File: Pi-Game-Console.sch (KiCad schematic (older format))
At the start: 108 parts, among them J1 Conn_01x02_Female, J10 Conn_01x04_Female, J2 FPC_Connector, J3 Conn_Coaxial, J4 AudioJack3_Ground_SwitchTR, J5 Micro_SD_Card, J6 CAM1, J7 USB_A, J8 USB_A, J9 Conn_01x04_Female, SW1 SW_DIP_x01, SW10 Y_Button, SW11 D_PAD_UP_Button, SW12 D_PAD_DOWN_Button, SW13 D_PAD_LEFT_Button, SW14 D_PAD_RIGHT_Button, SW2 Home_Button, SW3 Start_Button, SW4 Select_Button, SW5 L_Button, SW6 R_Button, SW7 A_Button, SW8 B_Button, SW9 X_Button, U1 UDA1334ATS, U2 TDA2822, U3 FAN5333BSX, U4 AR1100, U5 ATmega32U4-AU, U6 FE1.1s, Y1 12MHz, Y2 16MHz, Y3 12MHz

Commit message: Fixed footprints, added PWM to display backlight
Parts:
- removed D1: 1N4148, Diode_SMD:D_0805_2012Metric, symbol Device:D
- removed J10, J9: Conn_01x04_Female, Connector_Molex:Molex_CLIK-Mate_502585-0470_1x04-1MP_P1.50mm_Horizontal, symbol Connector:Conn_01x04_Female
- removed JP2: SolderJumper_2_Open, Jumper:SolderJumper-2_P1.3mm_Open_TrianglePad1.0x1.5mm, symbol Jumper:SolderJumper_2_Open
- removed R14: 20k, Resistor_SMD:R_0805_2012Metric, symbol Device:R
- removed R18: 67, Resistor_SMD:R_0805_2012Metric, symbol Device:R
- removed RV1: R_POT, Potentiometer_SMD:Potentiometer_Bourns_3214G_Horizontal, symbol Device:R_POT
- added J10, J9: Conn_01x05_Female, Connector_FFC-FPC:Molex_200528-0050_1x05-1MP_P1.00mm_Horizontal, symbol Connector:Conn_01x05_Female
- added RV2: R_POT, Potentiometer_SMD:Potentiometer_Bourns_3269P_Horizontal, symbol Device:R_POT
- SW10, SW11, SW12, SW13, SW14, SW2, SW3, SW4, SW5, SW6, SW7, SW8, SW9: footprint Button_Switch_SMD:SW_Push_1P1T_NO_6x6mm_H9.5mm -> Button_Switch_THT:SW_PUSH_6mm_H5mm
- renumbered D2 to D1, D3 to D2, D4 to D3, JP3 to JP2, R15 to R14, R16 to R15, R17 to R16, R19 to R17, R20 to R18, R21 to R19, R22 to R20, R23 to R21
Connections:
- net +5V: now also J10.1 (Pin_1), J9.1 (Pin_1), RV2.1
- net GND: now also J10.3 (Pin_3), J9.3 (Pin_3), RV2.3
- net L_JOYSTICK_X: now also J9.2 (Pin_2)
- net L_JOYSTICK_Y: now also J9.4 (Pin_4)
- net R_JOYSTICK_X: now also J10.2 (Pin_2)
- net R_JOYSTICK_Y: now also J10.4 (Pin_4)
- net DISP_PWM: now reaches U5.12 (PB7)
- net DISP_PWM: now also U3.4 (~SHDN)
- net DISP_PWM_POT: now reaches U5.40 (PF1)
- net DISP_PWM_POT: now also RV2.2
- net R_JOYSTICK_BTN: now reaches U5.41 (PF0)
- net R_JOYSTICK_BTN: now also J10.5 (Pin_5)
- net L_JOYSTICK_BTN: now reaches U5.8 (PB0)
- net L_JOYSTICK_BTN: now also J9.5 (Pin_5)
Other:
- note added: "DISPLAY BACKLIGHT CONTROL"
- note added: "JOYSTICK PINOUTS ARE NOT YET VALID"
- moved on the sheet: J7, J8, JP2, R17

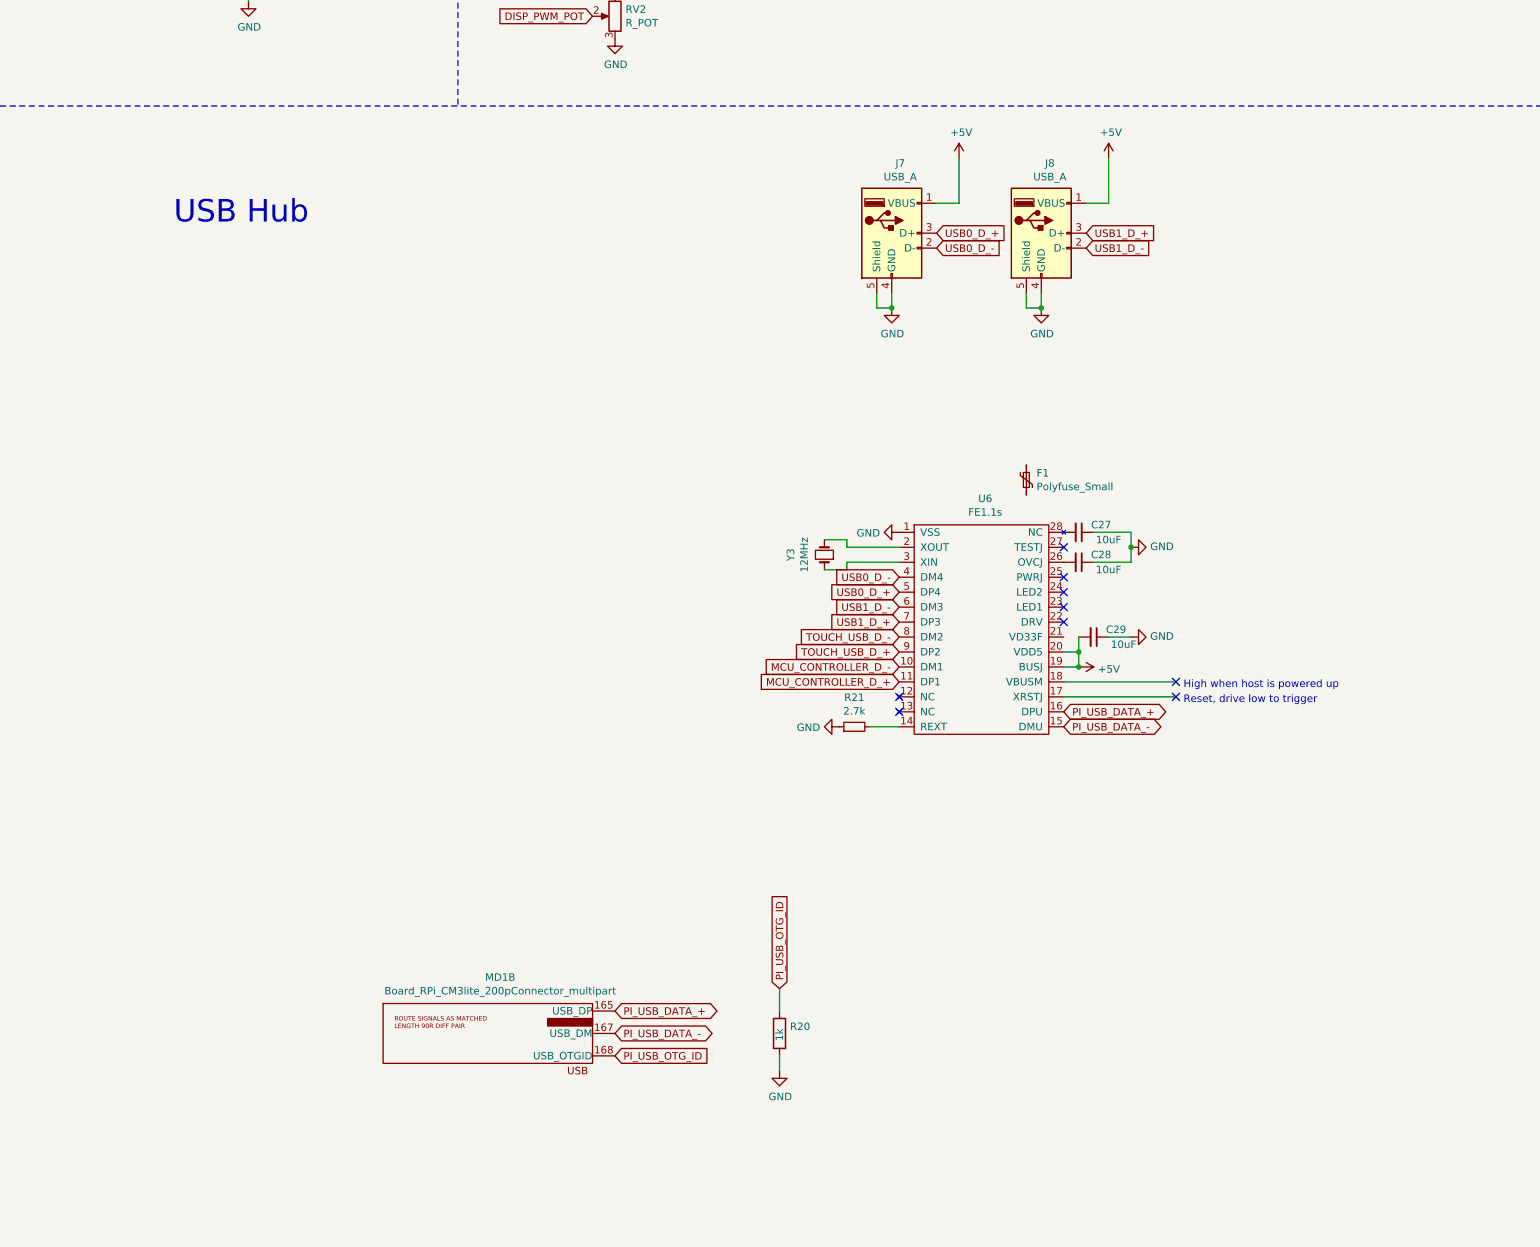
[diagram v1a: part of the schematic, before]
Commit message: Added Buck Converters for Power
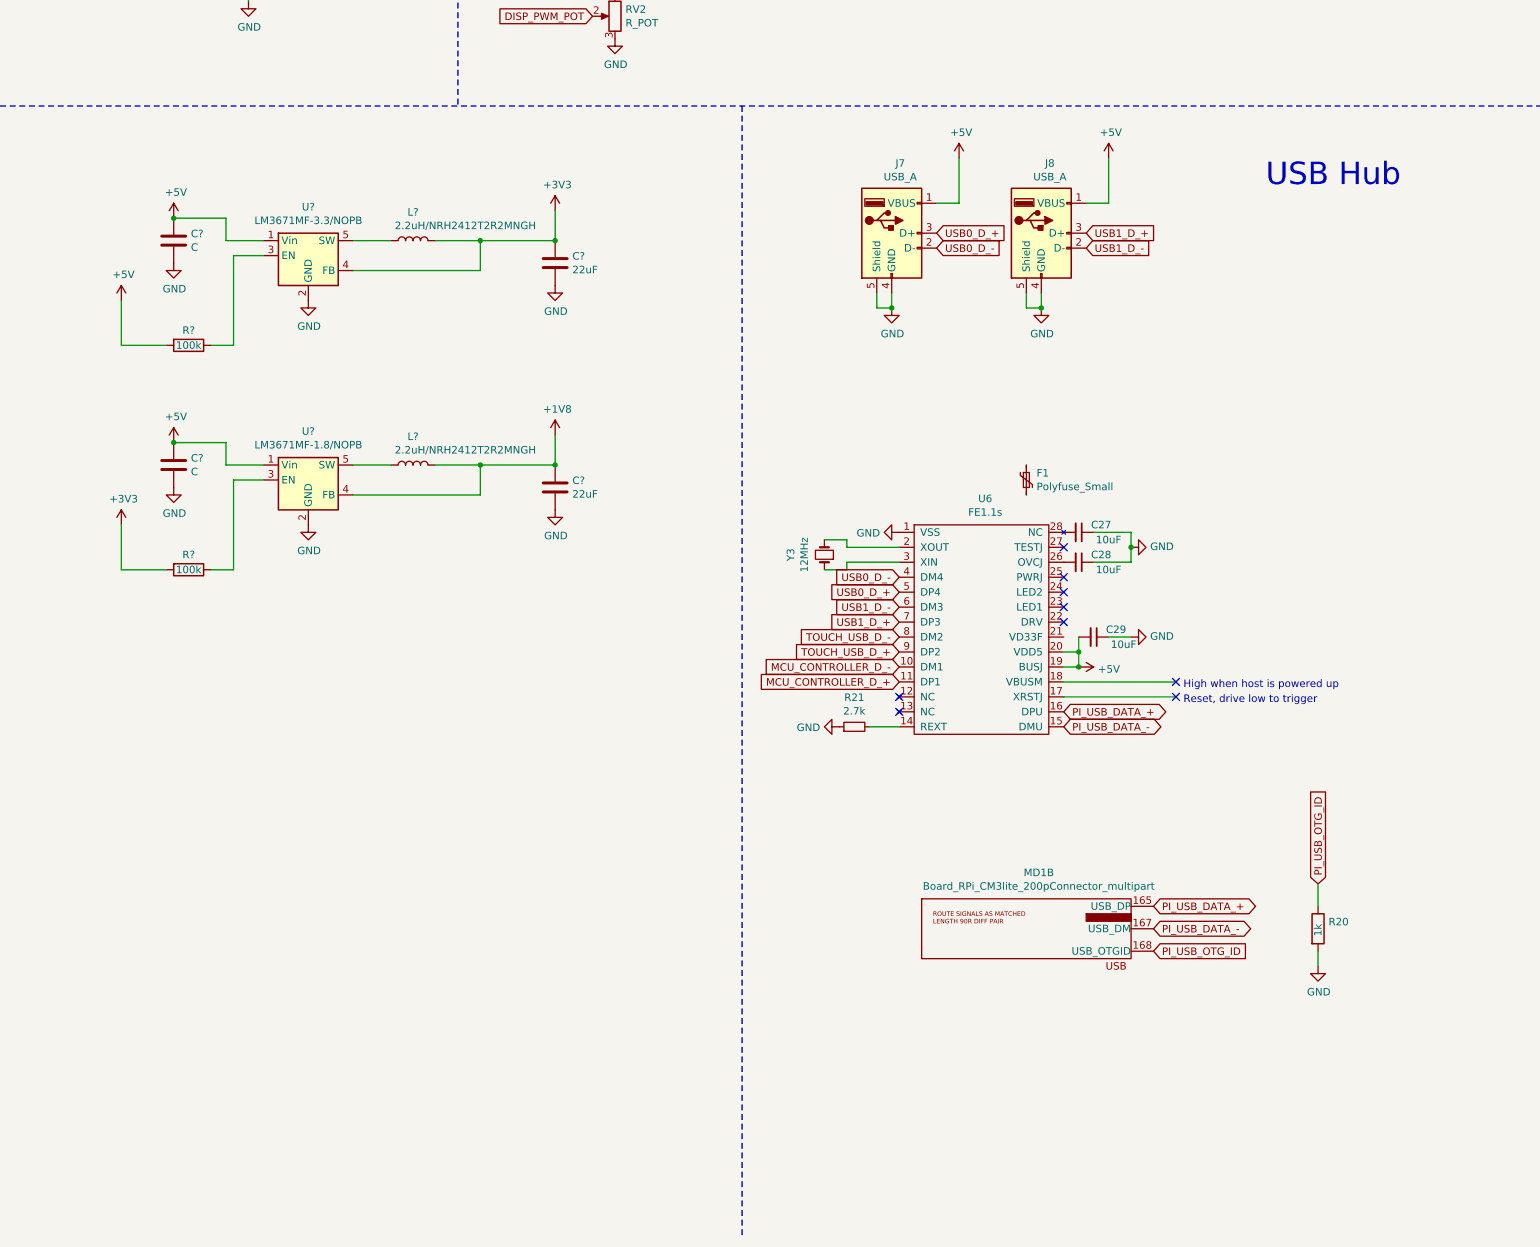
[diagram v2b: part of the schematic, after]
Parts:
- added C? (x2): 22uF, symbol Device:C
- added C? (x2): C, symbol Device:C
- added L? (x2): 2.2uH/NRH2412T2R2MNGH, symbol Device:L
- added R? (x2): 100k, symbol Device:R
- added U?: LM3671MF-3.3/NOPB, Package_TO_SOT_SMD:TSOT-23-5, symbol Regulator_Switching:LM3670MF
- added U?: LM3671MF-1.8/NOPB, Package_TO_SOT_SMD:TSOT-23-5, symbol Regulator_Switching:LM3670MF
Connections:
- net +1V8: now also C?.1, L?.2, U?.4 (FB)
- net +3V3: now also C?.1, L?.2, R?.2, U?.4 (FB)
- net +5V: now also C?.1, C?.1, R?.2, U?.1 (Vin), U?.1 (Vin)
- net GND: now also C?.2, C?.2, C?.2, C?.2, U?.2 (GND), U?.2 (GND)
- new net: R?.1, U?.3 (EN) (x2)
- new net: L?.1, U?.5 (SW) (x2)
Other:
- moved on the sheet: MD1B, R20

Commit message: Updated values for several parts
Mostly capacitors.  Still need to do further review the schematic before it's all the way finished.
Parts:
- C10, C11: value 0.01uF -> 10nF
- C15, C16: value C_Small -> 20pF
- C21, C5, C6: value 0.1uF -> 100nF
- C22, C23: renamed from C?; value C -> 10uF
- C24: renamed from C22; value 0.1uF -> 100nF
- C30: renamed from C26; value C_Small -> 10uF
- gave numbers to parts that had none: 8
- renumbered C23 to C27, C24 to C28, C25 to C29, C27 to C31, C28 to C32, C29 to C33, R19 to R21, R21 to R22, R20 to R23, RV2 to RV1, U5 to U7, U6 to U8

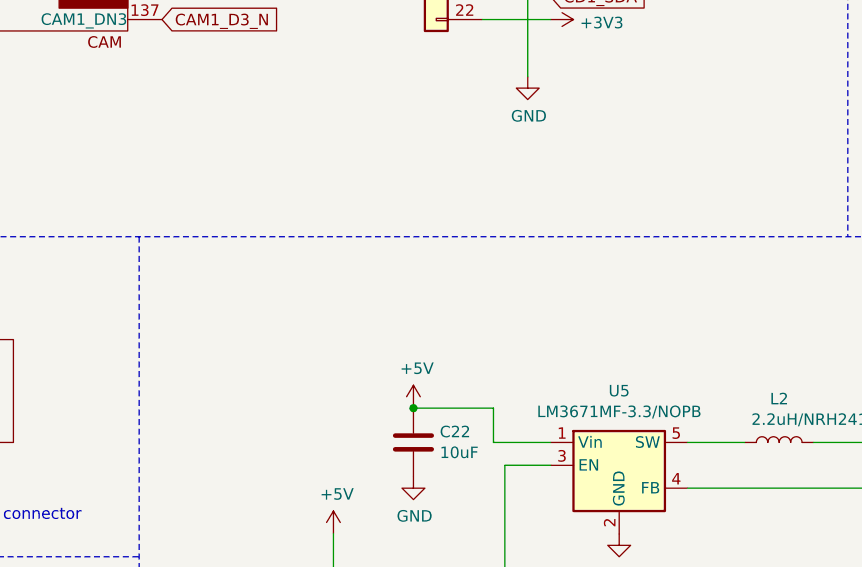
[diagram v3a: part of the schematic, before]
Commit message: Added more part values
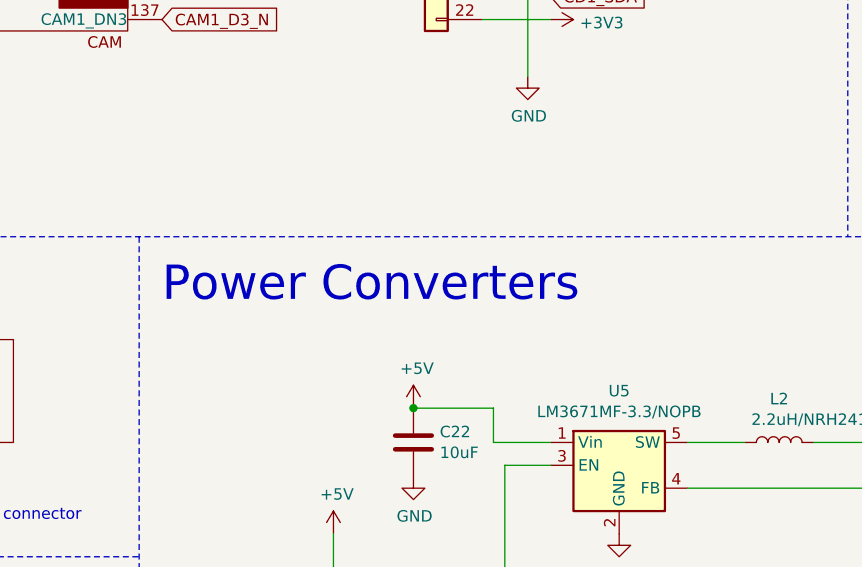
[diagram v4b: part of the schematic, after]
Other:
- note added: "Power Converters"
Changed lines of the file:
@@
 	1    0    0    -1
 $EndComp
+Text Notes 12750 8900 0    150  ~ 0
+Power Converters
 $EndSCHEMATC
